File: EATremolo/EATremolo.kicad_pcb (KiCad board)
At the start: 2 copper layers, 0 parts

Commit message: EA Tremolo Layout completed
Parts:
- added C1: 47nF, C_Disc_2mmPads:C_Disc_2mmPads, F.Cu at (94.3, 132.5)
- added C2: 1uF, CP_Radial_D4_P2_PadSize2_Drill1:CP_Radial_D4_P2_PadSize2_Drill1, F.Cu at (97.1, 89.1)
- added C3: 1uF, CP_Radial_D4_P2_PadSize2_Drill1:CP_Radial_D4_P2_PadSize2_Drill1, F.Cu at (92.4, 91.1)
- added C4: 1uF, CP_Radial_D4_P2_PadSize2_Drill1:CP_Radial_D4_P2_PadSize2_Drill1, F.Cu at (93.6, 94.3)
- added C5: 10uF, C_Disc_P5:C_Disc_P5.0mm_2mmPads, F.Cu at (60.2, 130.8)
- added C6: 220nF, C_Disc_2mmPads:C_Disc_2mmPads, F.Cu at (67.3, 125.8)
- added C7: 470nF, C_Disc_P5:C_Disc_P5.0mm_2mmPads, F.Cu at (69.2, 114.9)
- added C8: 470nF, C_Disc_2mmPads:C_Disc_2mmPads, F.Cu at (86.3, 89.3)
- added C9: 10uF, CP_Radial_D4_P2_PadSize2_Drill1:CP_Radial_D4_P2_PadSize2_Drill1, F.Cu at (82.6, 54.9)
- added CHASIS_EARTH1: CONN_01X01, Wire_Pads:SolderWirePad_single_1mmDrill, F.Cu at (76.5, 50.4)
- added D2: D_Schottky, Diodes_THT:D_DO-41_SOD81_P2.54mm_Vertical_AnodeUp, F.Cu at (75.9, 62.2)
- added DRATE1: LED, LEDs:LED_D5.0mm, F.Cu at (78.2, 87.5)
- added J1: JACK__MONO_2P_NC, custom_sockets:JackSocket_Mono_PCB, F.Cu at (90.2, 108.2)
- added J2: BARREL_JACK, Connectors:BARREL_JACK, F.Cu at (69.1, 61.7)
- added J3: JACK__MONO_2P_NC, custom_sockets:JackSocket_Mono_PCB, F.Cu at (66.5, 101.3)
- added Q1: Q_NJFET_DSG, TO_SOT_Packages_SMD:SOT-23_Handsoldering, F.Cu at (90.0, 138.3)
- added Q2: Q_NPN_EBC, Q_NPN_EBC_PadSize2_Drill1:TO-92_Inline_Wide, F.Cu at (89.2, 97.2)
- added Q3: Q_NPN_EBC, Q_NPN_EBC_PadSize2_Drill1:TO-92_Inline_Wide, F.Cu at (66.3, 120.9)
- added Q4: Q_NJFET_DSG, TO_SOT_Packages_SMD:SOT-23_Handsoldering, F.Cu at (88.5, 53.3)
- added R1: 1M, R_Axial_DIN0207_Vertical_2mmPad:R_Axial_DIN0207_Vertical_2mmPad, F.Cu at (94.3, 123.9)
- added R10: 4.7K, R_Axial_DIN0207_Vertical_2mmPad:R_Axial_DIN0207_Vertical_2mmPad, F.Cu at (58.8, 117.0)
- added R11: 180R, Resistors_THT:R_Axial_DIN0207_L6.3mm_D2.5mm_P5.08mm_Vertical, F.Cu at (81.9, 58.3)
- added R12: 180R, R_Axial_DIN0207_Vertical_2mmPad:R_Axial_DIN0207_Vertical_2mmPad, F.Cu at (85.6, 60.9)
- added R13: 68k, R_Axial_DIN0207_Vertical_2mmPad:R_Axial_DIN0207_Vertical_2mmPad, F.Cu at (89.7, 60.9)
- added R14: 100K, R_Axial_DIN0207_Vertical_2mmPad:R_Axial_DIN0207_Vertical_2mmPad, F.Cu at (96.4, 60.9)
- added R15: 100K, R_Axial_DIN0207_Vertical_2mmPad:R_Axial_DIN0207_Vertical_2mmPad, F.Cu at (93.4, 60.9)
- added R2: 1M, R_Axial_DIN0207_Vertical_2mmPad:R_Axial_DIN0207_Vertical_2mmPad, F.Cu at (67.1, 138.3)
- added R3: 1M, R_Axial_DIN0207_Vertical_2mmPad:R_Axial_DIN0207_Vertical_2mmPad, F.Cu at (97.5, 123.9)
- added R4: 15K, R_Axial_DIN0207_Vertical_2mmPad:R_Axial_DIN0207_Vertical_2mmPad, F.Cu at (97.1, 96.3)
- added R5: 10K, R_Axial_DIN0207_P5:R_Axial_DIN0207_P5.08mm_2mmPads, F.Cu at (97.4, 133.6)
- added R6: 2.2M, R_Axial_DIN0207_Vertical_2mmPad:R_Axial_DIN0207_Vertical_2mmPad, F.Cu at (84.7, 94.8)
- added R7: 560K, R_Axial_DIN0207_Vertical_2mmPad:R_Axial_DIN0207_Vertical_2mmPad, F.Cu at (64.8, 130.4)
- added R8: 150K, R_Axial_DIN0207_Vertical_2mmPad:R_Axial_DIN0207_Vertical_2mmPad, F.Cu at (68.6, 118.6)
- added R9: 10K, R_Axial_DIN0207_Vertical_2mmPad:R_Axial_DIN0207_Vertical_2mmPad, F.Cu at (81.0, 92.2)
- added RATE1: B100K, Potentiometers:Potentiometer_Omeg_PC16PU_Horizontal, F.Cu at (93.7, 86.1)
- added SW1: SW_3PDT_on_on, custom_sw:SW_3PDT_W18MM_L17.3MM_P5.3MM_D2MM, F.Cu at (78.2, 128.5)
- added VOL1: A25K, Potentiometers:Potentiometer_Omeg_PC16PU_Horizontal, F.Cu at (72.9, 86.1)
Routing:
- net /GND: track 0.00 -> 323.8 mm
- net /+9V: track 0.00 -> 203.8 mm, vias 0 -> 4
- net Net-(Q3-Pad1): track 0.00 -> 69.4 mm, vias 0 -> 2
- net Net-(SW1-Pad9): track 0.00 -> 66.8 mm, vias 0 -> 2
- net Net-(J1-Pad1): track 0.00 -> 57.1 mm
- net Net-(R9-Pad2): track 0.00 -> 55.1 mm
- net Net-(C1-Pad1): track 0.00 -> 47.5 mm
- net Net-(C7-Pad1): track 0.00 -> 42.3 mm
- net Net-(C8-Pad1): track 0.00 -> 37.8 mm
- net Net-(J3-Pad1): track 0.00 -> 34.8 mm, vias 0 -> 2
- net Net-(C1-Pad2): track 0.00 -> 27.2 mm
- net Net-(C3-Pad1): track 0.00 -> 21.7 mm
- net Net-(C6-Pad1): track 0.00 -> 18.9 mm
- net Net-(C2-Pad1): track 0.00 -> 14.5 mm
- net Net-(D2-Pad2): track 0.00 -> 10.0 mm
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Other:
- board outline added: 44.5 x 94.2 mm

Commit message: EA Tremolo Rev2
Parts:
- added R16: 1K, R_Axial_DIN0207_Vertical_2mmPad:R_Axial_DIN0207_Vertical_2mmPad, F.Cu at (96.6, 90.8)
- C2, C3, C4: footprint CP_Radial_D4_P2_PadSize2_Drill1:CP_Radial_D4_P2_PadSize2_Drill1 -> C_Disc_2mmPads:C_Disc_2mmPads
- R11: footprint Resistors_THT:R_Axial_DIN0207_L6.3mm_D2.5mm_P5.08mm_Vertical -> R_Axial_DIN0207_P5:R_Axial_DIN0207_P5.08mm_2mmPads
- R12: value 180R -> 1.2K
- R14: value 100K -> 180K
- moved R2 6.56 mm to (67.3, 131.7), turned to 180 degrees
- moved C3 5.55 mm to (86.9, 90.2), turned to 0 degrees
- moved C2 4.50 mm to (92.7, 90.2)
- moved J2 3.88 mm to (71.3, 58.5)
- moved C8 2.72 mm to (83.7, 90.2), turned to 270 degrees
- moved CHASIS_EARTH1 2.59 mm to (78.5, 52.1)
- moved Q1 2.49 mm to (90.2, 135.8), turned to 90 degrees
- moved R1 2.04 mm to (93.2, 122.1)
- moved R7 1.93 mm to (64.8, 128.5)
- moved R9 1.87 mm to (79.6, 91.0)
- moved DRATE1 1.79 mm to (78.3, 85.7), turned to 270 degrees
- moved R5 1.66 mm to (96.3, 132.3)
- moved C1 1.63 mm to (93.2, 131.3)
- moved R6 1.61 mm to (83.9, 96.1), turned to 180 degrees
- moved Q2 1.59 mm to (88.3, 98.6)
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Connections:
- C5 pad 1: /+9V -> Net-(C5-Pad1)
- DRATE1 pad 1: Net-(DRATE1-Pad1) -> Net-(C3-Pad1)
- DRATE1 pad 2: Net-(C3-Pad1) -> Net-(DRATE1-Pad2)
- Q1 pad 2: Net-(Q1-Pad2) -> Net-(C5-Pad1)
- R5 pad 1: Net-(Q1-Pad2) -> Net-(C5-Pad1)
- R9 pad 1: Net-(DRATE1-Pad1) -> Net-(DRATE1-Pad2)
- RATE1 pad 2: Net-(C2-Pad1) -> Net-(R16-Pad2)
- RATE1 pad 3: Net-(C2-Pad1) -> Net-(R16-Pad2)
- SW1 pad 1: /GND -> Net-(SW1-Pad1)
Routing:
- net Net-(C5-Pad1): track 0.00 -> 46.1 mm
- net /GND: track 323.8 -> 296.6 mm, vias 0 -> 2
- net Net-(R16-Pad2): track 0.00 -> 13.8 mm
- net /+9V: track 203.8 -> 190.3 mm
- net Net-(Q1-Pad2): track 7.71 -> 0.00 mm
- net Net-(DRATE1-Pad1): track 6.74 -> 0.00 mm
- net Net-(C2-Pad1): track 14.5 -> 8.56 mm
- net Net-(C1-Pad1): track 47.5 -> 51.4 mm
- net Net-(DRATE1-Pad2): track 0.00 -> 3.32 mm
- net Net-(SW1-Pad1): track 0.00 -> 1.96 mm
- net Net-(J3-Pad1): track 34.8 -> 36.6 mm
- net Net-(C6-Pad1): track 18.9 -> 17.2 mm
- net Net-(C3-Pad1): track 21.7 -> 22.9 mm
- net Net-(C1-Pad2): track 27.2 -> 28.2 mm
- net Net-(D2-Pad2): track 10.0 -> 9.09 mm
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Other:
- board size 44.5 x 94.2 mm -> 42.4 x 96.5 mm

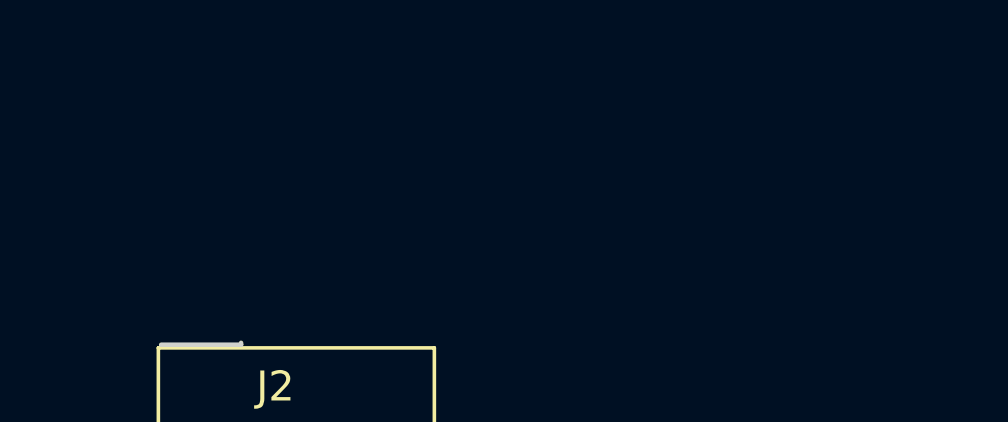
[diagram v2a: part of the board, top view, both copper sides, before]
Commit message: Board Description Updates
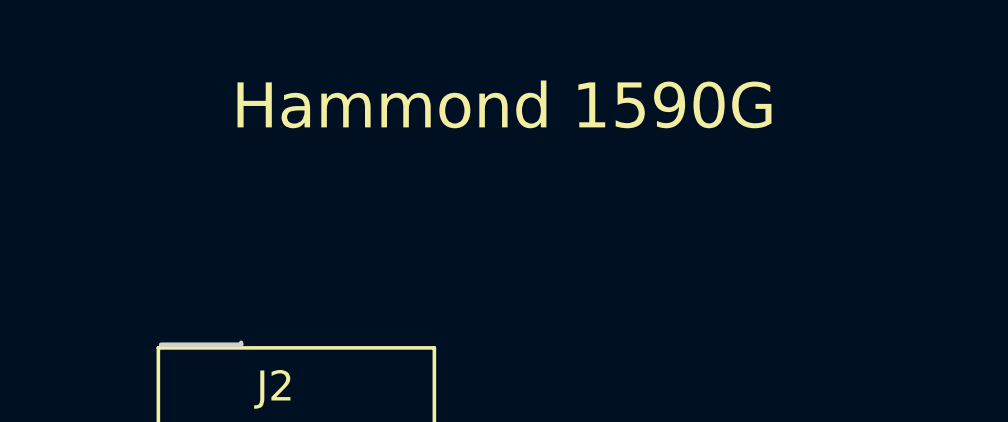
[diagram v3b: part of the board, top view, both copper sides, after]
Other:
- board text added: "Hammond 1590G"
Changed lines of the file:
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@@
     (links 60)
     (no_connects 0)
-    (area 57.074999 44.501999 99.643001 141.172001)
+    (area 45.444999 35.503 111.273001 144.077)
     (thickness 1.6)
-    (drawings 19)
+    (drawings 20)
     (tracks 393)
     (zones 0)
@@
   )
   (setup
-    (last_trace_width 0.5)
+    (last_trace_width 0.25)
     (user_trace_width 0.5)
     (user_trace_width 0.75)
@@
     )
   )
+  (gr_text "Hammond 1590G\n" (at 78.232 36.703) (layer F.SilkS)
+    (effects (font (size 1.5 1.5) (thickness 0.3)))
+  )
   (gr_line (start 69.469 44.6405) (end 69.469 44.577) (angle 90) (layer Edge.Cuts) (width 0.15))
